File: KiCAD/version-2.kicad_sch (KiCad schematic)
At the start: 19 parts, among them J1 batt. con., J2 circuit con., SW1 Power, Y1 12Mhz

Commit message: version 2
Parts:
- removed BT1: 4xAA, symbol Device:Battery
- removed C1, C3: 18pF, symbol Device:C
- removed C2, C5: 10uF, symbol Device:C_Polarized
- removed C4: 100nF, symbol Device:C
- removed C6: 1nF, symbol Device:C
- removed D1: 1N4001, Diode_THT:D_DO-41_SOD81_P10.16mm_Horizontal, symbol Diode:1N4001
- removed D2: GREEN LED, symbol Device:LED
- removed D3: 1N4148, Diode_THT:D_DO-35_SOD27_P7.62mm_Horizontal, symbol Diode:1N4148
- removed J1: batt. con., symbol Connector:Conn_01x02_Female
- removed J2: circuit con., symbol Connector:Conn_01x02_Male
- removed L1: 10mH, symbol Device:L
- removed LS1: 130 OHM, symbol Device:Speaker
- removed R1: 76, symbol Device:R
- removed R2: 5M1, symbol Device:R
- removed R3: 330, symbol Device:R
- removed SW1: Power, symbol Switch:SW_SPST
- removed Y1: 12Mhz, symbol Device:Crystal
- added BT?: 4xAA, symbol Device:Battery
- added C?: 1nF, symbol Device:C
- added C?: 100nF, symbol Device:C
- added C? (x2): 10uF, symbol Device:C_Polarized
- added D?: 1N4148, Diode_THT:D_DO-35_SOD27_P7.62mm_Horizontal, symbol Diode:1N4148
- added D?: GREEN LED, symbol Device:LED
- added D?: 1N4001, Diode_THT:D_DO-41_SOD81_P10.16mm_Horizontal, symbol Diode:1N4001
- added J?: batt. con., symbol Connector:Conn_01x02_Female
- added J?: circuit con., symbol Connector:Conn_01x02_Male
- added L?: 10mH, symbol Device:L
- added LS?: 130 OHM, symbol Device:Speaker
- added R?: 76, symbol Device:R
- added R?: 5M1, symbol Device:R
- added R?: 330, symbol Device:R
- added SW?: Power, symbol Switch:SW_SPST
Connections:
- net +6Volt: now also C?.1, D?.2 (A), J?.1 (Pin_1)
- net 5.3v: now also D?.1 (K)
- net A3: now also C?.2, D?.1 (K), R?.1
- net D4: now also C?.1
- net D6: now also R?.2
- net GND: now also C?.1, C?.2, D?.1 (K), J?.2 (Pin_2), L?.2, LS?.2, R?.2
- net T1CH4: now also R?.1
- new net: C?.1, D?.2 (A), R?.2
- new net: C?.2, L?.1
- new net: BT?.1 (+), SW?.1 (A)
- new net: BT?.2 (-), J?.2 (Pin_2)
- new net: J?.1 (Pin_1), SW?.2 (B)
- new net: D?.2 (A), R?.1
- new net: C?.2, LS?.1
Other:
- removed sheet version 2
- note added: "SB5 must be bridged on NUCLEO board"
- note removed: "metal-pointer Rev. 3"

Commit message: premier commit sur bare-metal
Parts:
- gave numbers to parts that had none: 16
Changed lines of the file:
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@@
   (symbol (lib_id "Device:C") (at 210.82 134.62 0) (unit 1)
     (in_bom yes) (on_board yes) (fields_autoplaced)
-    (property "Reference" "C?" (id 0) (at 214.63 133.3499 0)
+    (property "Reference" "C10" (id 0) (at 214.63 133.3499 0)
       (effects (font (size 1.27 1.27)) (justify left))
     )
@@
   (symbol (lib_id "power:GND") (at 147.32 158.75 0) (unit 1)
     (in_bom yes) (on_board yes) (fields_autoplaced)
-    (property "Reference" "#PWR?" (id 0) (at 147.32 165.1 0)
+    (property "Reference" "#PWR015" (id 0) (at 147.32 165.1 0)
       (effects (font (size 1.27 1.27)) hide)
     )
@@
   (symbol (lib_id "power:GND") (at 97.79 113.03 0) (unit 1)
     (in_bom yes) (on_board yes) (fields_autoplaced)
-    (property "Reference" "#PWR?" (id 0) (at 97.79 119.38 0)
+    (property "Reference" "#PWR011" (id 0) (at 97.79 119.38 0)
       (effects (font (size 1.27 1.27)) hide)
     )
@@
   (symbol (lib_id "Device:Battery") (at 68.58 114.3 0) (unit 1)
     (in_bom yes) (on_board yes) (fields_autoplaced)
-    (property "Reference" "BT?" (id 0) (at 72.39 112.6489 0)
+    (property "Reference" "BT2" (id 0) (at 72.39 112.6489 0)
       (effects (font (size 1.27 1.27)) (justify left))
     )
@@
   (symbol (lib_id "Diode:1N4148") (at 201.93 101.6 0) (unit 1)
     (in_bom yes) (on_board yes) (fields_autoplaced)
-    (property "Reference" "D?" (id 0) (at 201.93 95.25 0))
+    (property "Reference" "D6" (id 0) (at 201.93 95.25 0))
     (property "Value" "1N4148" (id 1) (at 201.93 97.79 0))
     (property "Footprint" "Diode_THT:D_DO-35_SOD27_P7.62mm_Horizontal" (id 2) (at 201.93 106.045 0)
@@
   (symbol (lib_id "power:GND") (at 156.21 93.98 180) (unit 1)
     (in_bom yes) (on_board yes) (fields_autoplaced)
-    (property "Reference" "#PWR?" (id 0) (at 156.21 87.63 0)
+    (property "Reference" "#PWR016" (id 0) (at 156.21 87.63 0)
       (effects (font (size 1.27 1.27)) hide)
     )
@@
   (symbol (lib_id "Connector:Conn_01x02_Female") (at 88.9 101.6 0) (unit 1)
     (in_bom yes) (on_board yes)
-    (property "Reference" "J?" (id 0) (at 86.36 106.68 0)
+    (property "Reference" "J3" (id 0) (at 86.36 106.68 0)
       (effects (font (size 1.27 1.27)) (justify left))
     )
@@
   (symbol (lib_id "Device:R") (at 152.4 146.05 90) (unit 1)
     (in_bom yes) (on_board yes) (fields_autoplaced)
-    (property "Reference" "R?" (id 0) (at 152.4 139.7 90))
+    (property "Reference" "R4" (id 0) (at 152.4 139.7 90))
     (property "Value" "76" (id 1) (at 152.4 142.24 90))
     (property "Footprint" "" (id 2) (at 152.4 147.828 90)
@@
   (symbol (lib_id "Device:C") (at 156.21 97.79 0) (unit 1)
     (in_bom yes) (on_board yes) (fields_autoplaced)
-    (property "Reference" "C?" (id 0) (at 160.02 96.5199 0)
+    (property "Reference" "C8" (id 0) (at 160.02 96.5199 0)
       (effects (font (size 1.27 1.27)) (justify left))
     )
@@
   (symbol (lib_id "power:GND") (at 135.89 105.41 180) (unit 1)
     (in_bom yes) (on_board yes)
-    (property "Reference" "#PWR?" (id 0) (at 135.89 99.06 0)
+    (property "Reference" "#PWR013" (id 0) (at 135.89 99.06 0)
       (effects (font (size 1.27 1.27)) hide)
     )
@@
   (symbol (lib_id "Device:C_Polarized") (at 167.64 147.32 0) (unit 1)
     (in_bom yes) (on_board yes) (fields_autoplaced)
-    (property "Reference" "C?" (id 0) (at 171.45 145.1609 0)
+    (property "Reference" "C9" (id 0) (at 171.45 145.1609 0)
       (effects (font (size 1.27 1.27)) (justify left))
     )
@@
   (symbol (lib_id "Device:LED") (at 147.32 154.94 90) (unit 1)
     (in_bom yes) (on_board yes)
-    (property "Reference" "D?" (id 0) (at 151.13 155.2574 90)
+    (property "Reference" "D5" (id 0) (at 151.13 155.2574 90)
       (effects (font (size 1.27 1.27)) (justify right))
     )
@@
   (symbol (lib_id "Connector:Conn_01x02_Male") (at 92.71 101.6 0) (unit 1)
     (in_bom yes) (on_board yes)
-    (property "Reference" "J?" (id 0) (at 92.71 106.68 0))
+    (property "Reference" "J4" (id 0) (at 92.71 106.68 0))
     (property "Value" "circuit con." (id 1) (at 96.52 99.06 0))
     (property "Footprint" "" (id 2) (at 92.71 101.6 0)
@@
   (symbol (lib_id "Device:R") (at 190.5 105.41 0) (unit 1)
     (in_bom yes) (on_board yes) (fields_autoplaced)
-    (property "Reference" "R?" (id 0) (at 193.04 104.1399 0)
+    (property "Reference" "R5" (id 0) (at 193.04 104.1399 0)
       (effects (font (size 1.27 1.27)) (justify left))
     )
@@
   (symbol (lib_id "power:GND") (at 167.64 165.1 0) (unit 1)
     (in_bom yes) (on_board yes)
-    (property "Reference" "#PWR?" (id 0) (at 167.64 171.45 0)
+    (property "Reference" "#PWR017" (id 0) (at 167.64 171.45 0)
       (effects (font (size 1.27 1.27)) hide)
     )
@@
   (symbol (lib_id "Device:Speaker") (at 172.72 157.48 0) (unit 1)
     (in_bom yes) (on_board yes) (fields_autoplaced)
-    (property "Reference" "LS?" (id 0) (at 177.8 157.4799 0)
+    (property "Reference" "LS2" (id 0) (at 177.8 157.4799 0)
       (effects (font (size 1.27 1.27)) (justify left))
     )
@@
   (symbol (lib_id "Diode:1N4001") (at 120.65 101.6 180) (unit 1)
     (in_bom yes) (on_board yes) (fields_autoplaced)
-    (property "Reference" "D?" (id 0) (at 120.65 95.25 0))
+    (property "Reference" "D4" (id 0) (at 120.65 95.25 0))
     (property "Value" "1N4001" (id 1) (at 120.65 97.79 0))
     (property "Footprint" "Diode_THT:D_DO-41_SOD81_P10.16mm_Horizontal" (id 2) (at 120.65 97.155 0)
@@
   (symbol (lib_id "Switch:SW_SPST") (at 73.66 101.6 0) (unit 1)
     (in_bom yes) (on_board yes) (fields_autoplaced)
-    (property "Reference" "SW?" (id 0) (at 73.66 95.25 0))
+    (property "Reference" "SW2" (id 0) (at 73.66 95.25 0))
     (property "Value" "Power" (id 1) (at 73.66 97.79 0))
     (property "Footprint" "" (id 2) (at 73.66 101.6 0)
@@
   (symbol (lib_id "power:GND") (at 142.24 134.62 0) (unit 1)
     (in_bom yes) (on_board yes) (fields_autoplaced)
-    (property "Reference" "#PWR?" (id 0) (at 142.24 140.97 0)
+    (property "Reference" "#PWR014" (id 0) (at 142.24 140.97 0)
       (effects (font (size 1.27 1.27)) hide)
     )
@@
   (symbol (lib_id "power:GND") (at 105.41 113.03 0) (unit 1)
     (in_bom yes) (on_board yes) (fields_autoplaced)
-    (property "Reference" "#PWR?" (id 0) (at 105.41 119.38 0)
+    (property "Reference" "#PWR012" (id 0) (at 105.41 119.38 0)
       (effects (font (size 1.27 1.27)) hide)
     )
@@
   (symbol (lib_id "power:GND") (at 190.5 109.22 0) (unit 1)
     (in_bom yes) (on_board yes) (fields_autoplaced)
-    (property "Reference" "#PWR?" (id 0) (at 190.5 115.57 0)
+    (property "Reference" "#PWR018" (id 0) (at 190.5 115.57 0)
       (effects (font (size 1.27 1.27)) hide)
     )
@@
   (symbol (lib_id "Device:L") (at 210.82 144.78 0) (unit 1)
     (in_bom yes) (on_board yes) (fields_autoplaced)
-    (property "Reference" "L?" (id 0) (at 212.09 143.5099 0)
+    (property "Reference" "L2" (id 0) (at 212.09 143.5099 0)
       (effects (font (size 1.27 1.27)) (justify left))
     )
@@
   (symbol (lib_id "power:GND") (at 210.82 148.59 0) (unit 1)
     (in_bom yes) (on_board yes) (fields_autoplaced)
-    (property "Reference" "#PWR?" (id 0) (at 210.82 154.94 0)
+    (property "Reference" "#PWR019" (id 0) (at 210.82 154.94 0)
       (effects (font (size 1.27 1.27)) hide)
     )
@@
   (symbol (lib_id "Device:C_Polarized") (at 105.41 109.22 0) (unit 1)
     (in_bom yes) (on_board yes) (fields_autoplaced)
-    (property "Reference" "C?" (id 0) (at 109.22 107.0609 0)
+    (property "Reference" "C7" (id 0) (at 109.22 107.0609 0)
       (effects (font (size 1.27 1.27)) (justify left))
     )
@@
   (symbol (lib_id "Device:R") (at 201.93 123.19 90) (unit 1)
     (in_bom yes) (on_board yes)
-    (property "Reference" "R?" (id 0) (at 201.93 120.65 90))
+    (property "Reference" "R6" (id 0) (at 201.93 120.65 90))
     (property "Value" "330" (id 1) (at 201.93 125.73 90))
     (property "Footprint" "" (id 2) (at 201.93 124.968 90)

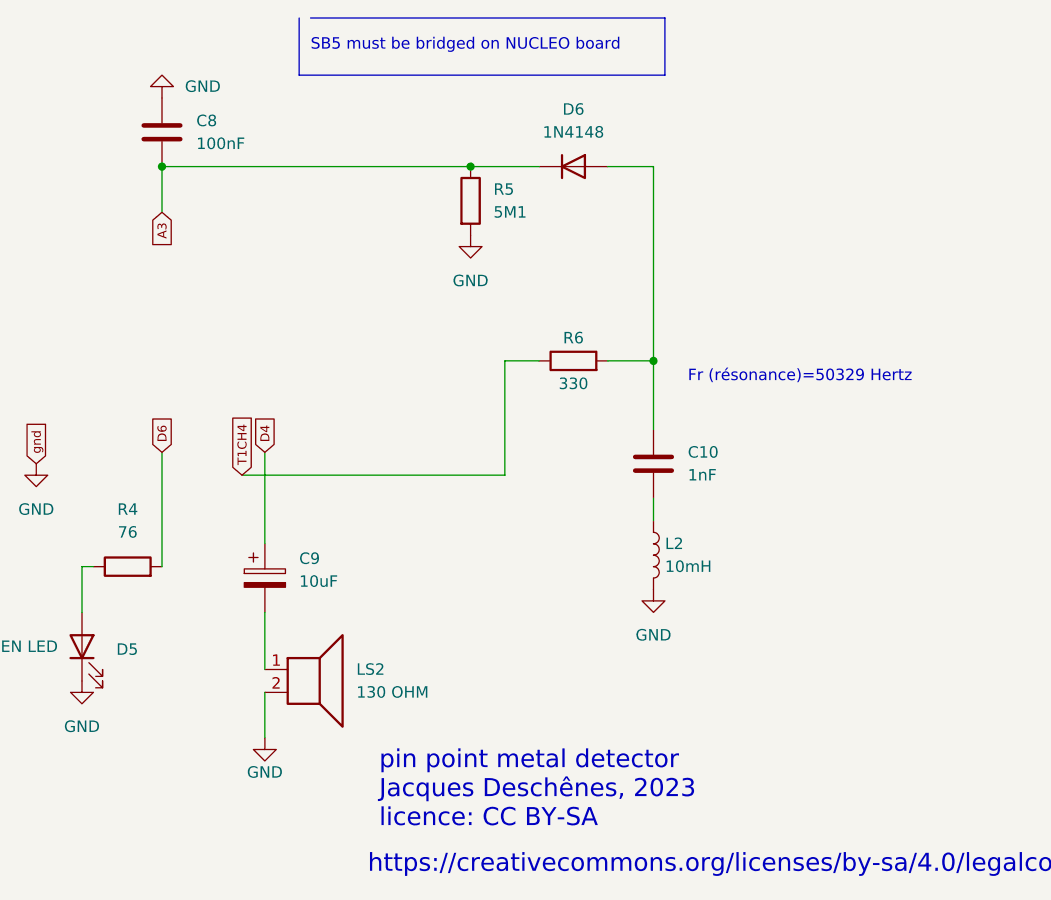
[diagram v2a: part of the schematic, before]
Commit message: modification à la version 2 et à metal-detector.bas
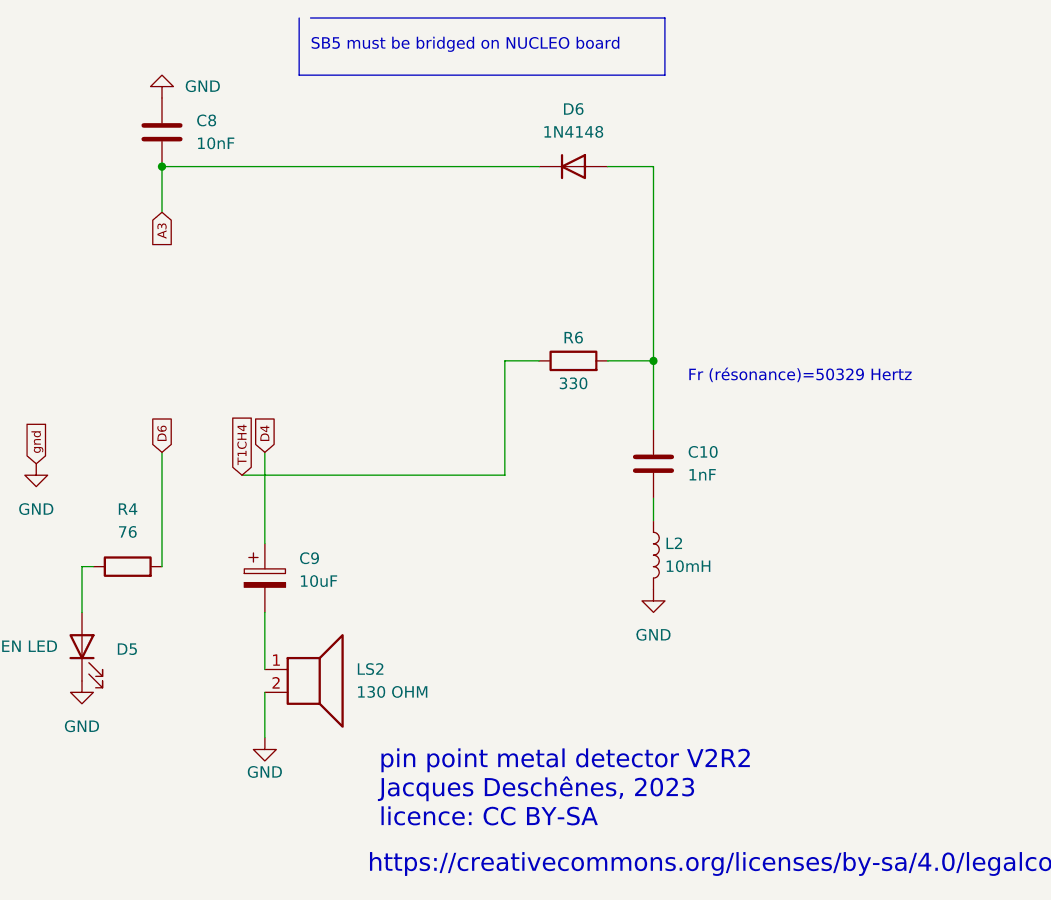
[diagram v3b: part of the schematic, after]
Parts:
- removed R5: 5M1, symbol Device:R
- C8: value 100nF -> 10nF
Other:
- note added: "pin point metal detector V2R2 Jacques Deschênes, 2023 licence: CC BY-SA"
- note removed: "pin point metal detector Jacques Deschênes, 2023 licence: CC BY-SA"
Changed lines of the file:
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@@
   (junction (at 156.21 101.6) (diameter 0) (color 0 0 0 0)
   )
-  (junction (at 190.5 101.6) (diameter 0) (color 0 0 0 0)
-  )
   (junction (at 113.03 101.6) (diameter 0) (color 0 0 0 0)
   )
@@
     (stroke (width 0) (type default) (color 0 0 0 0))
   )
-  (wire (pts (xy 190.5 101.6) (xy 198.12 101.6))
+  (wire (pts (xy 156.21 101.6) (xy 198.12 101.6))
     (stroke (width 0) (type default) (color 0 0 0 0))
   )
@@
     (stroke (width 0) (type default) (color 0 0 0 0))
   )
-  (wire (pts (xy 156.21 101.6) (xy 190.5 101.6))
-    (stroke (width 0) (type default) (color 0 0 0 0))
-  )
   (wire (pts (xy 68.58 101.6) (xy 68.58 109.22))
     (stroke (width 0) (type default) (color 0 0 0 0))
@@
     )
   )
-  (text "pin point metal detector\nJacques Deschênes, 2023\nlicence: CC BY-SA\n"
+  (text "pin point metal detector V2R2\nJacques Deschênes, 2023\nlicence: CC BY-SA\n"
     (at 180.34 175.26 0)
     (effects (font (size 2 2)) (justify left bottom))
@@
       (effects (font (size 1.27 1.27)) (justify left))
     )
-    (property "Value" "100nF" (id 1) (at 160.02 99.0599 0)
+    (property "Value" "10nF" (id 1) (at 160.02 99.0599 0)
       (effects (font (size 1.27 1.27)) (justify left))
     )
@@
     (pin "2")
   )
-  (symbol (lib_id "Device:R") (at 190.5 105.41 0) (unit 1)
-    (in_bom yes) (on_board yes) (fields_autoplaced)
-    (property "Reference" "R5" (id 0) (at 193.04 104.1399 0)
-      (effects (font (size 1.27 1.27)) (justify left))
-    )
-    (property "Value" "5M1" (id 1) (at 193.04 106.6799 0)
-      (effects (font (size 1.27 1.27)) (justify left))
-    )
-    (property "Footprint" "" (id 2) (at 188.722 105.41 90)
-      (effects (font (size 1.27 1.27)) hide)
-    )
-    (property "Datasheet" "~" (id 3) (at 190.5 105.41 0)
-      (effects (font (size 1.27 1.27)) hide)
-    )
-    (pin "1")
-    (pin "2")
-  )
   (symbol (lib_id "power:GND") (at 167.64 165.1 0) (unit 1)
     (in_bom yes) (on_board yes)
@@
       (effects (font (size 1.27 1.27)) hide)
     )
-    (pin "1")
-  )
-  (symbol (lib_id "power:GND") (at 190.5 109.22 0) (unit 1)
-    (in_bom yes) (on_board yes) (fields_autoplaced)
-    (property "Reference" "#PWR018" (id 0) (at 190.5 115.57 0)
-      (effects (font (size 1.27 1.27)) hide)
-    )
-    (property "Value" "GND" (id 1) (at 190.5 114.3 0))
-    (property "Footprint" "" (id 2) (at 190.5 109.22 0)
-      (effects (font (size 1.27 1.27)) hide)
-    )
-    (property "Datasheet" "" (id 3) (at 190.5 109.22 0)
-      (effects (font (size 1.27 1.27)) hide)
-    )

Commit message: circuit final choisi nail-finder.v7.png
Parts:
- renumbered R6 to R5
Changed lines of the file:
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@@
   (symbol (lib_id "power:GND") (at 210.82 148.59 0) (unit 1)
     (in_bom yes) (on_board yes) (fields_autoplaced)
-    (property "Reference" "#PWR019" (id 0) (at 210.82 154.94 0)
+    (property "Reference" "#PWR018" (id 0) (at 210.82 154.94 0)
       (effects (font (size 1.27 1.27)) hide)
     )
@@
   (symbol (lib_id "Device:R") (at 201.93 123.19 90) (unit 1)
     (in_bom yes) (on_board yes)
-    (property "Reference" "R6" (id 0) (at 201.93 120.65 90))
+    (property "Reference" "R5" (id 0) (at 201.93 120.65 90))
     (property "Value" "330" (id 1) (at 201.93 125.73 90))
     (property "Footprint" "" (id 2) (at 201.93 124.968 90)
